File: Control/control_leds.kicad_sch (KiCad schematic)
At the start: 32 parts

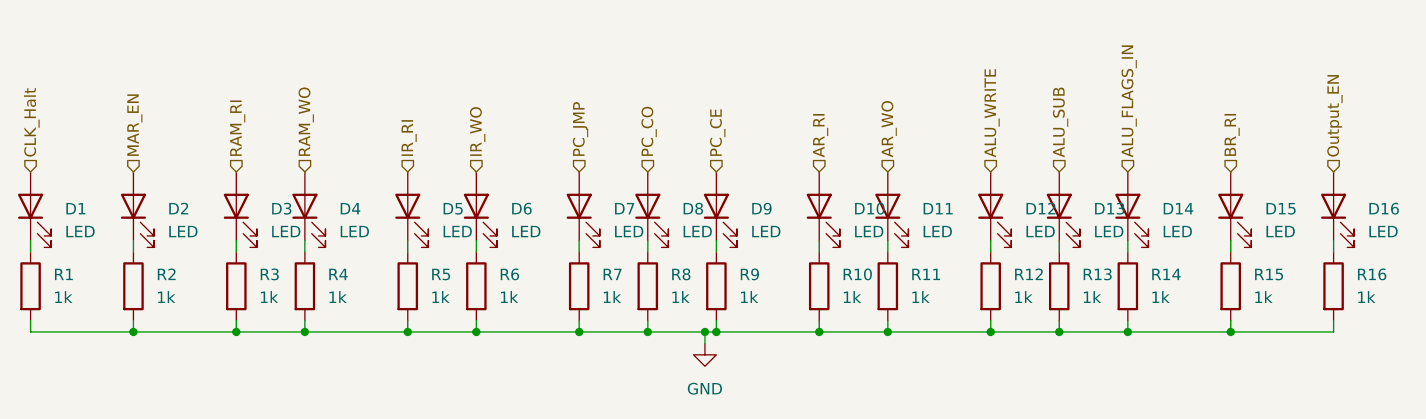
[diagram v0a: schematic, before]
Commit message: Control routed on PCB
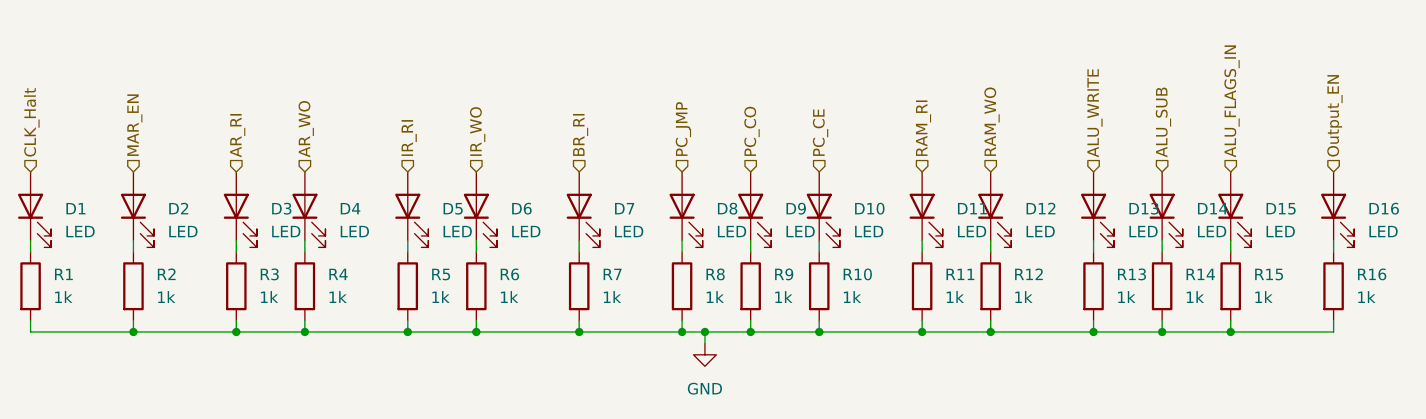
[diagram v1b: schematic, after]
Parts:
- D1, D10, D11, D12, D13, D14, D15, D16, D2, D3, D4, D5, D6, D7, D8, D9: footprint (none) -> LED_THT:LED_D5.0mm
- R1, R10, R11, R12, R13, R14, R15, R16, R2, R3, R4, R5, R6, R7, R8, R9: footprint (none) -> _DownloadFootprints:CF_series_Resistors_THT
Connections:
- net ALU_FLAGS_IN: now also D15.2 (A); no longer D14.2 (A)
- net ALU_SUB: now also D14.2 (A); no longer D13.2 (A)
- net ALU_WRITE: now also D13.2 (A); no longer D12.2 (A)
- net AR_RI: now also D3.2 (A); no longer D10.2 (A)
- net AR_WO: now also D4.2 (A); no longer D11.2 (A)
- net BR_RI: now also D7.2 (A); no longer D15.2 (A)
- net PC_CE: now also D10.2 (A); no longer D9.2 (A)
- net PC_CO: now also D9.2 (A); no longer D8.2 (A)
- net PC_JMP: now also D8.2 (A); no longer D7.2 (A)
- net RAM_RI: now also D11.2 (A); no longer D3.2 (A)
- net RAM_WO: now also D12.2 (A); no longer D4.2 (A)
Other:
- moved on the sheet: D11, D13, D14, D8, D9, R11, R13, R14, R8, R9

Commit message: Added spare pins to control
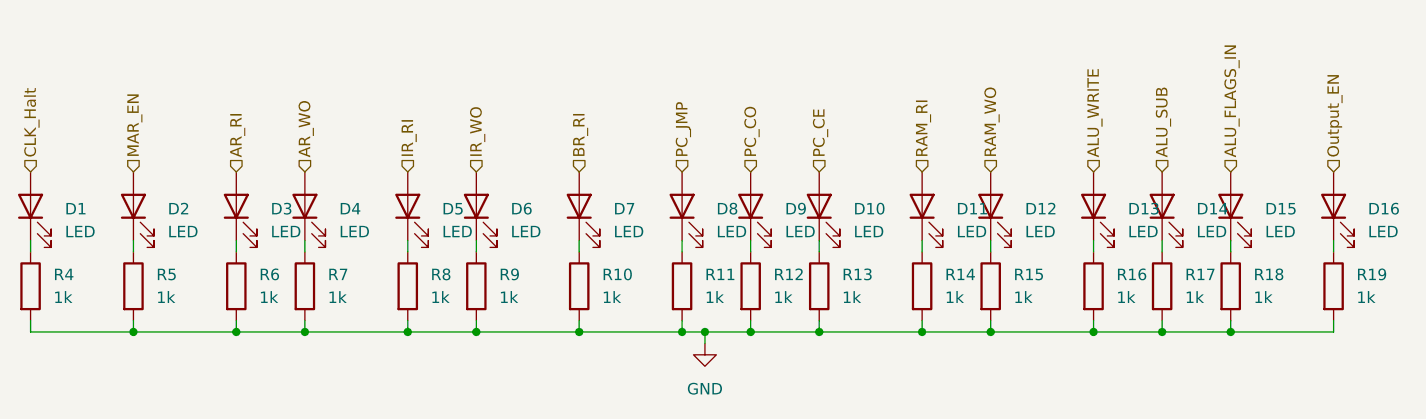
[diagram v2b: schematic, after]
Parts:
- renumbered R7 to R10, R8 to R11, R9 to R12, R10 to R13, R11 to R14, R12 to R15, R13 to R16, R14 to R17, R15 to R18, R16 to R19, R1 to R4, R2 to R5, R3 to R6, R4 to R7, R5 to R8, R6 to R9
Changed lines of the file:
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@@
 		(dnp no)
 		(fields_autoplaced yes)
-		(property "Reference" "R13"
+		(property "Reference" "R16"
 			(at 193.04 106.6799 0)
 			(effects
@@
 			(project "Control"
 				(path "/460bc1d8-5a70-4cad-87d6-3febe61be174/83729e76-58db-4276-abb5-f5827a97ab90"
-					(reference "R13")
+					(reference "R16")
 					(unit 1)
 				)
@@
 		(dnp no)
 		(fields_autoplaced yes)
-		(property "Reference" "R8"
+		(property "Reference" "R11"
 			(at 147.32 106.6799 0)
 			(effects
@@
 			(project "Control"
 				(path "/460bc1d8-5a70-4cad-87d6-3febe61be174/83729e76-58db-4276-abb5-f5827a97ab90"
-					(reference "R8")
+					(reference "R11")
 					(unit 1)
 				)
@@
 		(dnp no)
 		(fields_autoplaced yes)
-		(property "Reference" "R14"
+		(property "Reference" "R17"
 			(at 200.66 106.6799 0)
 			(effects
@@
 			(project "Control"
 				(path "/460bc1d8-5a70-4cad-87d6-3febe61be174/83729e76-58db-4276-abb5-f5827a97ab90"
-					(reference "R14")
+					(reference "R17")
 					(unit 1)
 				)
@@
 		(dnp no)
 		(fields_autoplaced yes)
-		(property "Reference" "R4"
+		(property "Reference" "R7"
 			(at 105.41 106.6799 0)
 			(effects
@@
 			(project "Control"
 				(path "/460bc1d8-5a70-4cad-87d6-3febe61be174/83729e76-58db-4276-abb5-f5827a97ab90"
-					(reference "R4")
+					(reference "R7")
 					(unit 1)
 				)
@@
 		(dnp no)
 		(fields_autoplaced yes)
-		(property "Reference" "#PWR025"
+		(property "Reference" "#PWR022"
 			(at 147.32 120.65 0)
 			(effects
@@
 			(project ""
 				(path "/460bc1d8-5a70-4cad-87d6-3febe61be174/83729e76-58db-4276-abb5-f5827a97ab90"
-					(reference "#PWR025")
+					(reference "#PWR022")
 					(unit 1)
 				)
@@
 		(dnp no)
 		(fields_autoplaced yes)
-		(property "Reference" "R10"
+		(property "Reference" "R13"
 			(at 162.56 106.6799 0)
 			(effects
@@
 			(project "Control"
 				(path "/460bc1d8-5a70-4cad-87d6-3febe61be174/83729e76-58db-4276-abb5-f5827a97ab90"
-					(reference "R10")
+					(reference "R13")
 					(unit 1)
 				)
@@
 		(dnp no)
 		(fields_autoplaced yes)
-		(property "Reference" "R12"
+		(property "Reference" "R15"
 			(at 181.61 106.6799 0)
 			(effects
@@
 			(project "Control"
 				(path "/460bc1d8-5a70-4cad-87d6-3febe61be174/83729e76-58db-4276-abb5-f5827a97ab90"
-					(reference "R12")
+					(reference "R15")
 					(unit 1)
 				)
@@
 		(dnp no)
 		(fields_autoplaced yes)
-		(property "Reference" "R5"
+		(property "Reference" "R8"
 			(at 116.84 106.6799 0)
 			(effects
@@
 			(project "Control"
 				(path "/460bc1d8-5a70-4cad-87d6-3febe61be174/83729e76-58db-4276-abb5-f5827a97ab90"
-					(reference "R5")
+					(reference "R8")
 					(unit 1)
 				)
@@
 		(dnp no)
 		(fields_autoplaced yes)
-		(property "Reference" "R7"
+		(property "Reference" "R10"
 			(at 135.89 106.6799 0)
 			(effects
@@
 			(project "Control"
 				(path "/460bc1d8-5a70-4cad-87d6-3febe61be174/83729e76-58db-4276-abb5-f5827a97ab90"
-					(reference "R7")
+					(reference "R10")
 					(unit 1)
 				)
@@
 		(dnp no)
 		(fields_autoplaced yes)
-		(property "Reference" "R16"
+		(property "Reference" "R19"
 			(at 219.71 106.6799 0)
 			(effects
@@
 			(project "Control"
 				(path "/460bc1d8-5a70-4cad-87d6-3febe61be174/83729e76-58db-4276-abb5-f5827a97ab90"
-					(reference "R16")
+					(reference "R19")
 					(unit 1)
 				)
@@
 		(dnp no)
 		(fields_autoplaced yes)
-		(property "Reference" "R3"
+		(property "Reference" "R6"
 			(at 97.79 106.6799 0)
 			(effects
@@
 			(project "Control"
 				(path "/460bc1d8-5a70-4cad-87d6-3febe61be174/83729e76-58db-4276-abb5-f5827a97ab90"
-					(reference "R3")
+					(reference "R6")
 					(unit 1)
 				)
@@
 		(dnp no)
 		(fields_autoplaced yes)
-		(property "Reference" "R2"
+		(property "Reference" "R5"
 			(at 86.36 106.6799 0)
 			(effects
@@
 			(project "Control"
 				(path "/460bc1d8-5a70-4cad-87d6-3febe61be174/83729e76-58db-4276-abb5-f5827a97ab90"
-					(reference "R2")
+					(reference "R5")
 					(unit 1)
 				)
@@
 		(dnp no)
 		(fields_autoplaced yes)
-		(property "Reference" "R11"
+		(property "Reference" "R14"
 			(at 173.99 106.6799 0)
 			(effects
@@
 			(project "Control"
 				(path "/460bc1d8-5a70-4cad-87d6-3febe61be174/83729e76-58db-4276-abb5-f5827a97ab90"
-					(reference "R11")
+					(reference "R14")
 					(unit 1)
 				)
@@
 		(dnp no)
 		(fields_autoplaced yes)
-		(property "Reference" "R1"
+		(property "Reference" "R4"
 			(at 74.93 106.6799 0)
 			(effects
@@
 			(project "Control"
 				(path "/460bc1d8-5a70-4cad-87d6-3febe61be174/83729e76-58db-4276-abb5-f5827a97ab90"
-					(reference "R1")
+					(reference "R4")
 					(unit 1)
 				)
@@
 		(dnp no)
 		(fields_autoplaced yes)
-		(property "Reference" "R6"
+		(property "Reference" "R9"
 			(at 124.46 106.6799 0)
 			(effects
@@
 			(project "Control"
 				(path "/460bc1d8-5a70-4cad-87d6-3febe61be174/83729e76-58db-4276-abb5-f5827a97ab90"
-					(reference "R6")
+					(reference "R9")
 					(unit 1)
 				)
@@
 		(dnp no)
 		(fields_autoplaced yes)
-		(property "Reference" "R9"
+		(property "Reference" "R12"
 			(at 154.94 106.6799 0)
 			(effects
@@
 			(project "Control"
 				(path "/460bc1d8-5a70-4cad-87d6-3febe61be174/83729e76-58db-4276-abb5-f5827a97ab90"
-					(reference "R9")
+					(reference "R12")
 					(unit 1)
 				)
@@
 		(dnp no)
 		(fields_autoplaced yes)
-		(property "Reference" "R15"
+		(property "Reference" "R18"
 			(at 208.28 106.6799 0)
 			(effects
@@
 			(project "Control"
 				(path "/460bc1d8-5a70-4cad-87d6-3febe61be174/83729e76-58db-4276-abb5-f5827a97ab90"
-					(reference "R15")
-					(unit 1)
-				)
+					(reference "R18")
+					(unit 1)
+				)
